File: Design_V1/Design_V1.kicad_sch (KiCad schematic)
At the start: 0 parts

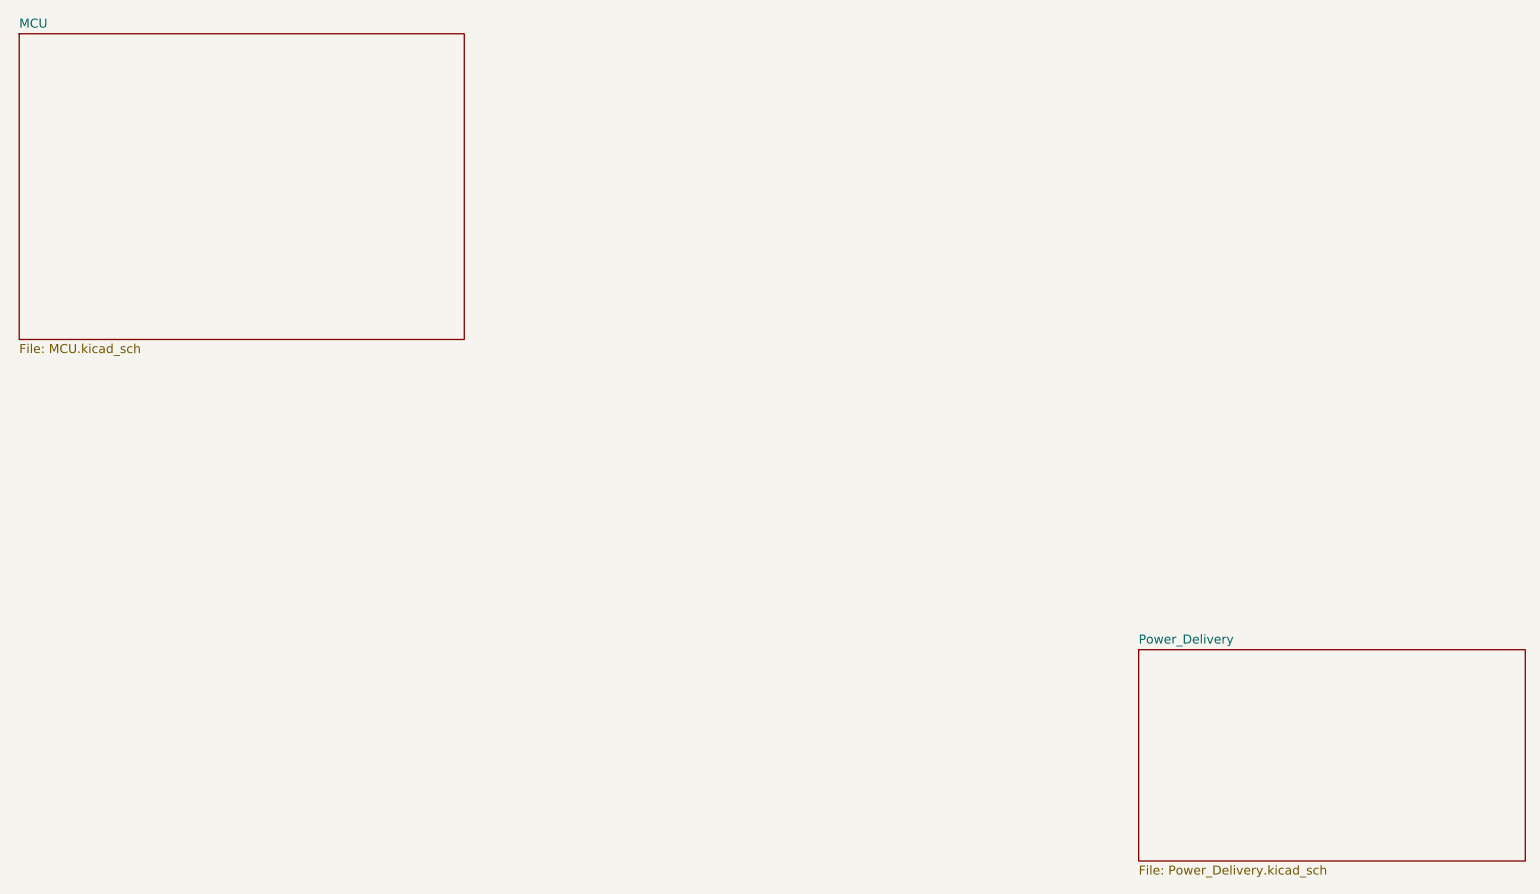
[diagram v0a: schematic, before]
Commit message: Updated Project. Added testpoints, crystal and jumpers. Added Power block
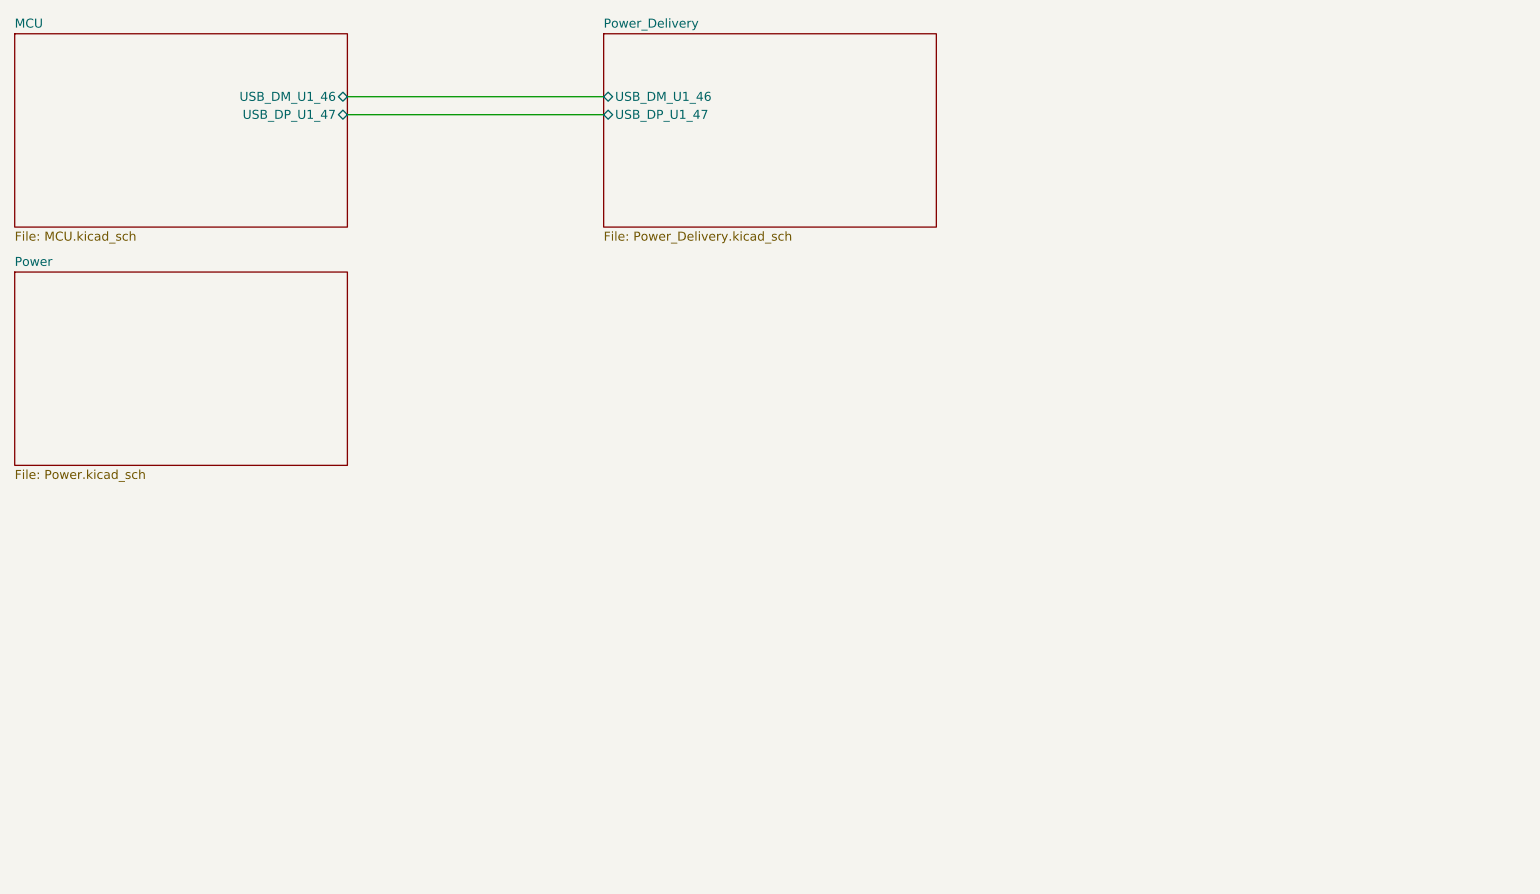
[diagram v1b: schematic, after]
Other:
- added sheet Power (Power.kicad_sch)
- sheet MCU ports: added USB_DM_U1_46, USB_DP_U1_47; removed none
- sheet Power_Delivery ports: added USB_DM_U1_46, USB_DP_U1_47; removed none
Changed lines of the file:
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@@
 (kicad_sch (version 20211123) (generator eeschema)
   (paper "A4")
-  (sheet (at 173.355 104.14) (size 54.61 29.845) (fields_autoplaced)
+  (wire (pts (xy 61.595 26.035) (xy 97.79 26.035))
+    (stroke (width 0) (type default) (color 0 0 0 0))
+  )
+  (wire (pts (xy 61.595 28.575) (xy 97.79 28.575))
+    (stroke (width 0) (type default) (color 0 0 0 0))
+  )
+  (sheet (at 14.605 50.8) (size 46.99 27.305) (fields_autoplaced)
     (stroke (width 0.1524) (type solid) (color 0 0 0 0))
     (fill (color 0 0 0 0.0000))
-    (property "Sheet name" "Power_Delivery" (id 0) (at 173.355 103.4284 0)
+    (property "Sheet name" "Power" (id 0) (at 14.605 50.0884 0)
       (effects (font (size 1.27 1.27)) (justify left bottom))
     )
-    (property "Sheet file" "Power_Delivery.kicad_sch" (id 1) (at 173.355 134.5696 0)
+    (property "Sheet file" "Power.kicad_sch" (id 1) (at 14.605 78.6896 0)
       (effects (font (size 1.27 1.27)) (justify left top))
     )
   )
-  (sheet (at 15.24 17.145) (size 62.865 43.18) (fields_autoplaced)
+  (sheet (at 97.79 17.145) (size 46.99 27.305) (fields_autoplaced)
     (stroke (width 0.1524) (type solid) (color 0 0 0 0))
     (fill (color 0 0 0 0.0000))
-    (property "Sheet name" "MCU" (id 0) (at 15.24 16.4334 0)
+    (property "Sheet name" "Power_Delivery" (id 0) (at 97.79 16.4334 0)
       (effects (font (size 1.27 1.27)) (justify left bottom))
     )
-    (property "Sheet file" "MCU.kicad_sch" (id 1) (at 15.24 60.9096 0)
+    (property "Sheet file" "Power_Delivery.kicad_sch" (id 1) (at 97.79 45.0346 0)
       (effects (font (size 1.27 1.27)) (justify left top))
+    )
+    (pin "USB_DM_U1_46" bidirectional (at 97.79 26.035 180)
+      (effects (font (size 1.27 1.27)) (justify left))
+    )
+    (pin "USB_DP_U1_47" bidirectional (at 97.79 28.575 180)
+      (effects (font (size 1.27 1.27)) (justify left))
+    )
+  )
+  (sheet (at 14.605 17.145) (size 46.99 27.305) (fields_autoplaced)
+    (stroke (width 0.1524) (type solid) (color 0 0 0 0))
+    (fill (color 0 0 0 0.0000))
+    (property "Sheet name" "MCU" (id 0) (at 14.605 16.4334 0)
+      (effects (font (size 1.27 1.27)) (justify left bottom))
+    )
+    (property "Sheet file" "MCU.kicad_sch" (id 1) (at 14.605 45.0346 0)
+      (effects (font (size 1.27 1.27)) (justify left top))
+    )
+    (pin "USB_DM_U1_46" bidirectional (at 61.595 26.035 0)
+      (effects (font (size 1.27 1.27)) (justify right))
+    )
+    (pin "USB_DP_U1_47" bidirectional (at 61.595 28.575 0)
+      (effects (font (size 1.27 1.27)) (justify right))
     )
   )
@@
     (path "/9bd6305a-703c-44bf-adb0-bbf4076617c8" (page "2"))
     (path "/6e813748-2b40-4644-b35c-2b86541cdcdc" (page "3"))
+    (path "/00fc787d-9f4e-47f5-90c9-6616c3a603eb" (page "4"))
   )
   (symbol_instances
+    (path "/9bd6305a-703c-44bf-adb0-bbf4076617c8/1ba42e76-6ddd-47f3-8197-e80738509081"
+      (reference "#FLG01") (unit 1) (value "PWR_FLAG") (footprint "")
+    )
     (path "/9bd6305a-703c-44bf-adb0-bbf4076617c8/f3b7bb4f-3c1d-4dfa-8749-a3a16444aa2b"
       (reference "#PWR01") (unit 1) (value "+3V3") (footprint "")
@@
       (reference "#PWR015") (unit 1) (value "GND") (footprint "")
     )
+    (path "/9bd6305a-703c-44bf-adb0-bbf4076617c8/75889c1e-ebfe-4f8a-a0fd-f78ba234a880"
+      (reference "#PWR016") (unit 1) (value "+1V1") (footprint "")
+    )
+    (path "/9bd6305a-703c-44bf-adb0-bbf4076617c8/7b7f9fb7-94f5-4b6f-92d1-a90115f34e63"
+      (reference "#PWR017") (unit 1) (value "GND") (footprint "")
+    )
+    (path "/9bd6305a-703c-44bf-adb0-bbf4076617c8/55148585-015b-4192-888b-33d9d8c4ed88"
+      (reference "#PWR018") (unit 1) (value "GND") (footprint "")
+    )
+    (path "/9bd6305a-703c-44bf-adb0-bbf4076617c8/f9a81e4e-7643-47b8-8032-cae03aee54b0"
+      (reference "#PWR019") (unit 1) (value "+3V3") (footprint "")
+    )
+    (path "/9bd6305a-703c-44bf-adb0-bbf4076617c8/8991f61e-b88d-4973-a810-e8e954cdf958"
+      (reference "#PWR020") (unit 1) (value "GND") (footprint "")
+    )
+    (path "/9bd6305a-703c-44bf-adb0-bbf4076617c8/b91bda52-6460-49fa-99e5-c72f142eabc3"
+      (reference "#PWR021") (unit 1) (value "+3V3") (footprint "")
+    )
+    (path "/9bd6305a-703c-44bf-adb0-bbf4076617c8/e020020a-70d6-4391-a24e-8f69fabea557"
+      (reference "#PWR022") (unit 1) (value "GND") (footprint "")
+    )
     (path "/9bd6305a-703c-44bf-adb0-bbf4076617c8/ed459d60-2755-4580-bbb0-62778a4d08b2"
       (reference "C1") (unit 1) (value "100nF") (footprint "")
@@
     )
     (path "/9bd6305a-703c-44bf-adb0-bbf4076617c8/81d740d4-e928-4d89-84a0-46fd1c241569"
-      (reference "C9") (unit 1) (value "100nF") (footprint "")
+      (reference "C9") (unit 1) (value "1uF") (footprint "")
     )
     (path "/9bd6305a-703c-44bf-adb0-bbf4076617c8/2eb47dfd-c43f-4f80-87dc-ac67518c8284"
       (reference "C10") (unit 1) (value "100nF") (footprint "")
     )
-    (path "/9bd6305a-703c-44bf-adb0-bbf4076617c8/3cda2794-a109-443a-89ca-fa2a5745b7d6"
-      (reference "J1") (unit 1) (value "Conn_02x03_Counter_Clockwise") (footprint "")
+    (path "/9bd6305a-703c-44bf-adb0-bbf4076617c8/e0fda225-ee14-450f-b790-0556939a6a8b"
+      (reference "C11") (unit 1) (value "100nF") (footprint "")
+    )
+    (path "/9bd6305a-703c-44bf-adb0-bbf4076617c8/0a63badf-c7b1-424b-b451-1f381ae5d2e6"
+      (reference "C12") (unit 1) (value "100nF") (footprint "")
+    )
+    (path "/9bd6305a-703c-44bf-adb0-bbf4076617c8/0ba84243-70c7-48df-bdf9-a84868bb200d"
+      (reference "C13") (unit 1) (value "1uF") (footprint "")
+    )
+    (path "/9bd6305a-703c-44bf-adb0-bbf4076617c8/5b35bf9a-9013-4dc9-b3c3-371e481d9e79"
+      (reference "J1") (unit 1) (value "Conn_02x04_Odd_Even") (footprint "Connector_PinHeader_2.54mm:PinHeader_2x04_P2.54mm_Vertical_SMD")
+    )
+    (path "/9bd6305a-703c-44bf-adb0-bbf4076617c8/7cf547fd-1531-4a66-8381-61053c9e81c3"
+      (reference "JP1") (unit 1) (value "Jumper_2_Open") (footprint "")
     )
     (path "/9bd6305a-703c-44bf-adb0-bbf4076617c8/2b4b3aab-2e48-45d2-8a72-cb5124256832"
@@
       (reference "R2") (unit 1) (value "27.3R") (footprint "")
     )
+    (path "/9bd6305a-703c-44bf-adb0-bbf4076617c8/ab135347-9bc1-4f54-a29c-1b3c4c120d06"
+      (reference "R3") (unit 1) (value "1K") (footprint "")
+    )
+    (path "/9bd6305a-703c-44bf-adb0-bbf4076617c8/f774874f-eb78-4c1e-9f3c-7a2ee1247e46"
+      (reference "R4") (unit 1) (value "1K") (footprint "")
+    )
+    (path "/9bd6305a-703c-44bf-adb0-bbf4076617c8/e7a44a9c-f24e-4658-baac-a7214ddc78df"
+      (reference "R5") (unit 1) (value "DNF") (footprint "")
+    )
+    (path "/9bd6305a-703c-44bf-adb0-bbf4076617c8/4f7d8c71-9c89-47e1-bdd9-71ea2ff9470f"
+      (reference "TP1") (unit 1) (value "TestPoint") (footprint "")
+    )
+    (path "/9bd6305a-703c-44bf-adb0-bbf4076617c8/3bd260bb-8cfd-410d-87e0-9c278a4b5279"
+      (reference "TP2") (unit 1) (value "TestPoint") (footprint "")
+    )
+    (path "/9bd6305a-703c-44bf-adb0-bbf4076617c8/f282391a-04e5-4ea1-b1f7-0f676a2a6f52"
+      (reference "TP3") (unit 1) (value "TestPoint") (footprint "")
+    )
+    (path "/9bd6305a-703c-44bf-adb0-bbf4076617c8/e0594f27-9b55-44c7-bc6a-8a8ae7963af4"
+      (reference "TP4") (unit 1) (value "TestPoint") (footprint "")
+    )
+    (path "/9bd6305a-703c-44bf-adb0-bbf4076617c8/89396a7a-d68d-419d-b8e2-5131e2b04c47"
+      (reference "TP5") (unit 1) (value "TestPoint") (footprint "")
+    )
+    (path "/9bd6305a-703c-44bf-adb0-bbf4076617c8/ada72aa7-edfd-4159-bfb2-b28ae12d33b8"
+      (reference "TP6") (unit 1) (value "TestPoint") (footprint "")
+    )
+    (path "/9bd6305a-703c-44bf-adb0-bbf4076617c8/44cc4e42-4f73-4ff9-9a9d-cbdd3d742887"
+      (reference "TP7") (unit 1) (value "TestPoint") (footprint "")
+    )
+    (path "/9bd6305a-703c-44bf-adb0-bbf4076617c8/3ef7964c-03a5-4095-af61-839f53edc68f"
+      (reference "TP8") (unit 1) (value "TestPoint") (footprint "")
+    )
+    (path "/9bd6305a-703c-44bf-adb0-bbf4076617c8/253c8a06-b588-4fdc-a80f-0660562f6bba"
+      (reference "TP9") (unit 1) (value "TestPoint") (footprint "")
+    )
+    (path "/9bd6305a-703c-44bf-adb0-bbf4076617c8/bdefc53a-5353-4439-9c63-53881107889a"
+      (reference "TP10") (unit 1) (value "TestPoint") (footprint "")
+    )
     (path "/9bd6305a-703c-44bf-adb0-bbf4076617c8/059a25d5-3bbc-4f56-9c32-a549d48d221c"
       (reference "U1") (unit 1) (value "RP2040") (footprint "Footprints:QFN40P700X700X90-57N")
@@
       (reference "USB1") (unit 1) (value "CSP-USC16-TR") (footprint "Footprints:VALCON_CSP-USC16-TR")
     )
-  )
+    (path "/9bd6305a-703c-44bf-adb0-bbf4076617c8/5be222b4-bb6b-4064-8da4-b859bd025adf"
+      (reference "Y1") (unit 1) (value "Crystal") (footprint "")
+    )
+  )

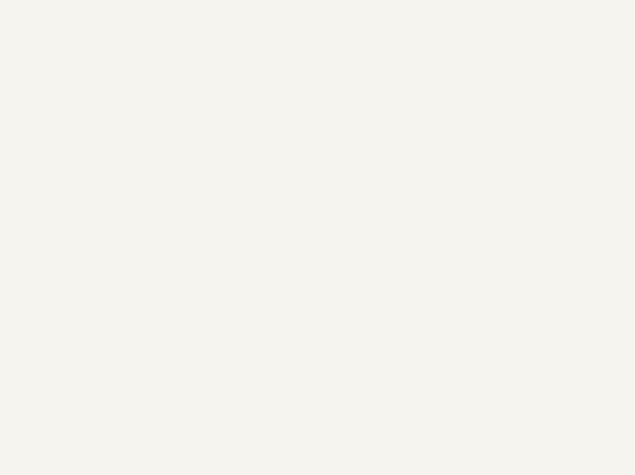
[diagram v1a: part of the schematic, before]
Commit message: Added Ethernet block
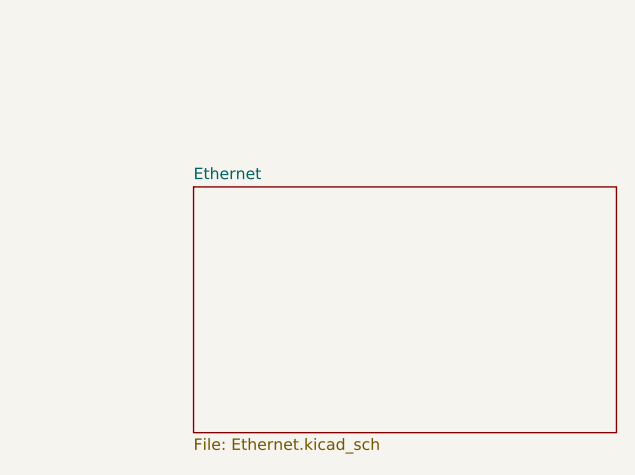
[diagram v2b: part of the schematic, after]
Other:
- added sheet Ethernet (Ethernet.kicad_sch)
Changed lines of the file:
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@@
+    )
+  )
+  (sheet (at 117.475 68.58) (size 46.99 27.305) (fields_autoplaced)
+    (stroke (width 0.1524) (type solid) (color 0 0 0 0))
+    (fill (color 0 0 0 0.0000))
+    (property "Sheet name" "Ethernet" (id 0) (at 117.475 67.8684 0)
+      (effects (font (size 1.27 1.27)) (justify left bottom))
+    )
+    (property "Sheet file" "Ethernet.kicad_sch" (id 1) (at 117.475 96.4696 0)
+      (effects (font (size 1.27 1.27)) (justify left top))
     )
   )
@@
     (path "/6e813748-2b40-4644-b35c-2b86541cdcdc" (page "3"))
     (path "/00fc787d-9f4e-47f5-90c9-6616c3a603eb" (page "4"))
+    (path "/71070041-e598-4cf8-9b6e-932bbf134d95" (page "5"))
   )
   (symbol_instances
@@
       (reference "#PWR022") (unit 1) (value "GND") (footprint "")
     )
+    (path "/71070041-e598-4cf8-9b6e-932bbf134d95/0f0a0e63-7610-4ec0-9a93-ce6a0a6d1a36"
+      (reference "#PWR023") (unit 1) (value "+3V3") (footprint "")
+    )
+    (path "/71070041-e598-4cf8-9b6e-932bbf134d95/d450e131-6d41-4c06-b863-15dd53404d2f"
+      (reference "#PWR024") (unit 1) (value "GND") (footprint "")
+    )
+    (path "/71070041-e598-4cf8-9b6e-932bbf134d95/a24f2879-62d0-4511-9ea7-29ac4a3e1309"
+      (reference "#PWR025") (unit 1) (value "+3.3VA") (footprint "")
+    )
+    (path "/71070041-e598-4cf8-9b6e-932bbf134d95/f219f056-9bb7-4d30-8789-cf781989bbf6"
+      (reference "#PWR026") (unit 1) (value "GND") (footprint "")
+    )
+    (path "/71070041-e598-4cf8-9b6e-932bbf134d95/8ecd61f3-b01c-49a2-ad64-8aff93cbf0b3"
+      (reference "#PWR027") (unit 1) (value "GND") (footprint "")
+    )
+    (path "/71070041-e598-4cf8-9b6e-932bbf134d95/6fb3ec46-d0c1-4a87-b385-222f8b7ae040"
+      (reference "#PWR028") (unit 1) (value "GND") (footprint "")
+    )
+    (path "/71070041-e598-4cf8-9b6e-932bbf134d95/d1a6795c-d991-404e-b44f-c232534ba52d"
+      (reference "#PWR029") (unit 1) (value "+1V8") (footprint "")
+    )
+    (path "/71070041-e598-4cf8-9b6e-932bbf134d95/7418d2e0-8530-4316-92ec-ca204aea76fb"
+      (reference "#PWR030") (unit 1) (value "GND") (footprint "")
+    )
+    (path "/71070041-e598-4cf8-9b6e-932bbf134d95/5c49fd7a-27b9-492e-8c57-22d9e843b4a3"
+      (reference "#PWR031") (unit 1) (value "+3V3") (footprint "")
+    )
+    (path "/71070041-e598-4cf8-9b6e-932bbf134d95/8ceb7a0c-4f67-4923-b168-192b34572727"
+      (reference "#PWR032") (unit 1) (value "GND") (footprint "")
+    )
+    (path "/71070041-e598-4cf8-9b6e-932bbf134d95/1eae1a2d-ac41-43c4-bf1b-bae560ef5d87"
+      (reference "#PWR033") (unit 1) (value "+3V3") (footprint "")
+    )
+    (path "/71070041-e598-4cf8-9b6e-932bbf134d95/36a622e5-4091-4a5e-bae0-b659b4043931"
+      (reference "#PWR034") (unit 1) (value "+3.3VA") (footprint "")
+    )
     (path "/9bd6305a-703c-44bf-adb0-bbf4076617c8/ed459d60-2755-4580-bbb0-62778a4d08b2"
       (reference "C1") (unit 1) (value "100nF") (footprint "")
@@
       (reference "C13") (unit 1) (value "1uF") (footprint "")
     )
+    (path "/71070041-e598-4cf8-9b6e-932bbf134d95/9ed5f09d-f428-462b-978c-7a9dd8637c06"
+      (reference "C14") (unit 1) (value "10uF") (footprint "")
+    )
+    (path "/71070041-e598-4cf8-9b6e-932bbf134d95/baf9f715-90ae-4e2f-bb63-fff113f601a4"
+      (reference "C15") (unit 1) (value "10uF") (footprint "")
+    )
+    (path "/71070041-e598-4cf8-9b6e-932bbf134d95/d0740029-b1f5-4b26-836d-50cd9bb4d30a"
+      (reference "C16") (unit 1) (value "10uF") (footprint "")
+    )
+    (path "/71070041-e598-4cf8-9b6e-932bbf134d95/5401cfac-fac2-4f7a-99b9-c38bdccd8eb2"
+      (reference "C17") (unit 1) (value "10uF") (footprint "")
+    )
+    (path "/71070041-e598-4cf8-9b6e-932bbf134d95/eef78ae0-346c-41d7-802e-11a4c2248e2d"
+      (reference "C18") (unit 1) (value "10uF") (footprint "")
+    )
+    (path "/71070041-e598-4cf8-9b6e-932bbf134d95/7c4b7d77-c40a-4911-a41b-ae64f912bffe"
+      (reference "C19") (unit 1) (value "10uF") (footprint "")
+    )
     (path "/9bd6305a-703c-44bf-adb0-bbf4076617c8/5b35bf9a-9013-4dc9-b3c3-371e481d9e79"
       (reference "J1") (unit 1) (value "Conn_02x04_Odd_Even") (footprint "Connector_PinHeader_2.54mm:PinHeader_2x04_P2.54mm_Vertical_SMD")
@@
       (reference "JP1") (unit 1) (value "Jumper_2_Open") (footprint "")
     )
+    (path "/71070041-e598-4cf8-9b6e-932bbf134d95/2ab5dd4f-b122-47f2-b4e0-735fc56e9921"
+      (reference "L1") (unit 1) (value "L") (footprint "")
+    )
+    (path "/71070041-e598-4cf8-9b6e-932bbf134d95/2a1b5ac3-a744-49dc-aee5-45861322be97"
+      (reference "L2") (unit 1) (value "L") (footprint "")
+    )
     (path "/9bd6305a-703c-44bf-adb0-bbf4076617c8/2b4b3aab-2e48-45d2-8a72-cb5124256832"
       (reference "R1") (unit 1) (value "27.3R") (footprint "")
@@
       (reference "U2") (unit 1) (value "W25Q128JVS") (footprint "Package_SO:SOIC-8_5.23x5.23mm_P1.27mm")
     )
+    (path "/71070041-e598-4cf8-9b6e-932bbf134d95/799905c4-4da0-4eb2-a63d-f04ebd0e3def"
+      (reference "U3") (unit 1) (value "W5100") (footprint "Package_QFP:LQFP-80_10x10mm_P0.4mm")
+    )
     (path "/6e813748-2b40-4644-b35c-2b86541cdcdc/fe008f65-7299-4999-a681-ba7df6d7c9ea"
